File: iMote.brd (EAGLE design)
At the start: 50 x 50 mm, 47 parts, among them CN1 C-02235, CN2 ICSP, CN3 CC-HEADER, IC1 ATmega328P-AU, IC2 FT232RLSSOP, IC3 BLE112-A-VISUAL, Q1 16MHz, T1 2SC1815

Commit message: 5cmx5cmにおさまった!
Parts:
- C10: device rcl:E2,5-5 -> my:E2-5
- moved S1 31.1 mm to (37.3, 5.79), turned to 0 degrees
- moved R4 28.4 mm to (32.3, 41.1)
- moved S2 23.4 mm to (43.6, 17.2), turned to 90 degrees
- moved C11 19.6 mm to (24.3, 25.4)
- moved R1 18.1 mm to (33.0, 10.1), turned to 180 degrees
- moved C2 17.8 mm to (4.14, 8.85), turned to 0 degrees
- moved C1 16.0 mm to (4.13, 14.0), turned to 0 degrees
- moved C5 14.1 mm to (25.5, 11.5), turned to 180 degrees
- moved C3 14.0 mm to (25.5, 13.1), turned to 180 degrees
- moved PL-IRM1 13.8 mm to (13.9, 5.50)
- moved R9 13.3 mm to (20.2, 5.40), turned to 0 degrees
- moved R8 12.6 mm to (11.6, 43.0)
- moved LED6 12.5 mm to (11.6, 46.3), turned to 90 degrees
- moved C12 11.5 mm to (17.9, 4.49), turned to 270 degrees
- moved SJ1 11.2 mm to (38.5, 47.0), turned to 0 degrees
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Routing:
- net GND: track 0.00 -> 101.4 mm, vias 0 -> 11
- net +5V: track 0.00 -> 88.7 mm
- net +3V3: track 0.00 -> 73.9 mm
- net !RESET: track 0.00 -> 41.4 mm, vias 0 -> 2
- net !BLE/RST: track 0.00 -> 35.6 mm, vias 0 -> 2
- net D6/BLERX: track 0.00 -> 24.2 mm, vias 0 -> 2
- net BLE/P2_2: track 0.00 -> 23.3 mm, vias 0 -> 2
- net D7/BLETX: track 0.00 -> 23.0 mm, vias 0 -> 2
- net D0/USBRX: track 0.00 -> 20.1 mm, vias 0 -> 2
- net BLE/P2_1: track 0.00 -> 20.1 mm, vias 0 -> 1
- net N$8: track 0.00 -> 16.5 mm, vias 0 -> 2
- net D1/USBTX: track 0.00 -> 15.7 mm
- net D12/MISO: track 0.00 -> 13.5 mm, vias 0 -> 2
- net D11/MOSI: track 0.00 -> 13.5 mm
- net N$2: track 0.00 -> 11.9 mm
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
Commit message: いい感じや
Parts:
- moved SJ1 6.18 mm to (37.4, 40.9), turned to 270 degrees
- moved LED3 4.99 mm to (44.5, 40.6), turned to 0 degrees
- moved R5 4.12 mm to (41.0, 40.5)
- moved R6 3.14 mm to (37.0, 19.5)
- moved LED4 3.02 mm to (37.0, 16.4)
- moved C6 2.53 mm to (19.4, 35.0), turned to 270 degrees
- moved S2 1.90 mm to (41.8, 16.6)
- moved R2 1.39 mm to (5.32, 41.4), turned to 90 degrees
- moved LED1 1.17 mm to (3.36, 41.4), turned to 270 degrees
- moved C11 1.10 mm to (25.4, 25.4)
- moved C8 0.22 mm to (44.5, 37.8)
- moved CN1 0.10 mm to (17.4, 44.5)
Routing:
- net GND: track 101.4 -> 70.0 mm, vias 11 -> 13
- net BLE/P2_1: track 20.1 -> 38.5 mm, vias 1 -> 0
- net USBD-: track 3.94 -> 19.1 mm
- net +5V: track 88.7 -> 97.5 mm
- net +3V3: track 73.9 -> 65.9 mm
- net !RESET: track 41.4 -> 46.5 mm
- net BLE/P0_0: track 5.90 -> 3.00 mm
- net !BLE/RST: track 35.6 -> 37.8 mm
- net USB/TXLED: track 9.54 -> 11.5 mm
- net D12/MISO: track 13.5 -> 11.7 mm, vias 2 -> 1
- net BLE/P2_2: track 23.3 -> 21.7 mm, vias 2 -> 1
- net D7/BLETX: track 23.0 -> 22.3 mm

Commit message: CN3ひっくり返したらもうちょいよくなった
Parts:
- moved SJ1 13.5 mm to (24.1, 38.7)
- moved R4 6.46 mm to (38.5, 42.9)
- moved CN3 1.69 mm to (29.4, 44.1), turned to 180 degrees
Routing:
- net BLE/P2_1: track 38.5 -> 11.9 mm, vias 0 -> 1
- net !BLE/RST: track 37.8 -> 56.5 mm, vias 2 -> 0
- net BLE/P2_2: track 21.7 -> 15.5 mm, vias 1 -> 0
- net PRG/VDD: track 3.86 -> 6.69 mm
- net +3V3: track 65.9 -> 63.9 mm

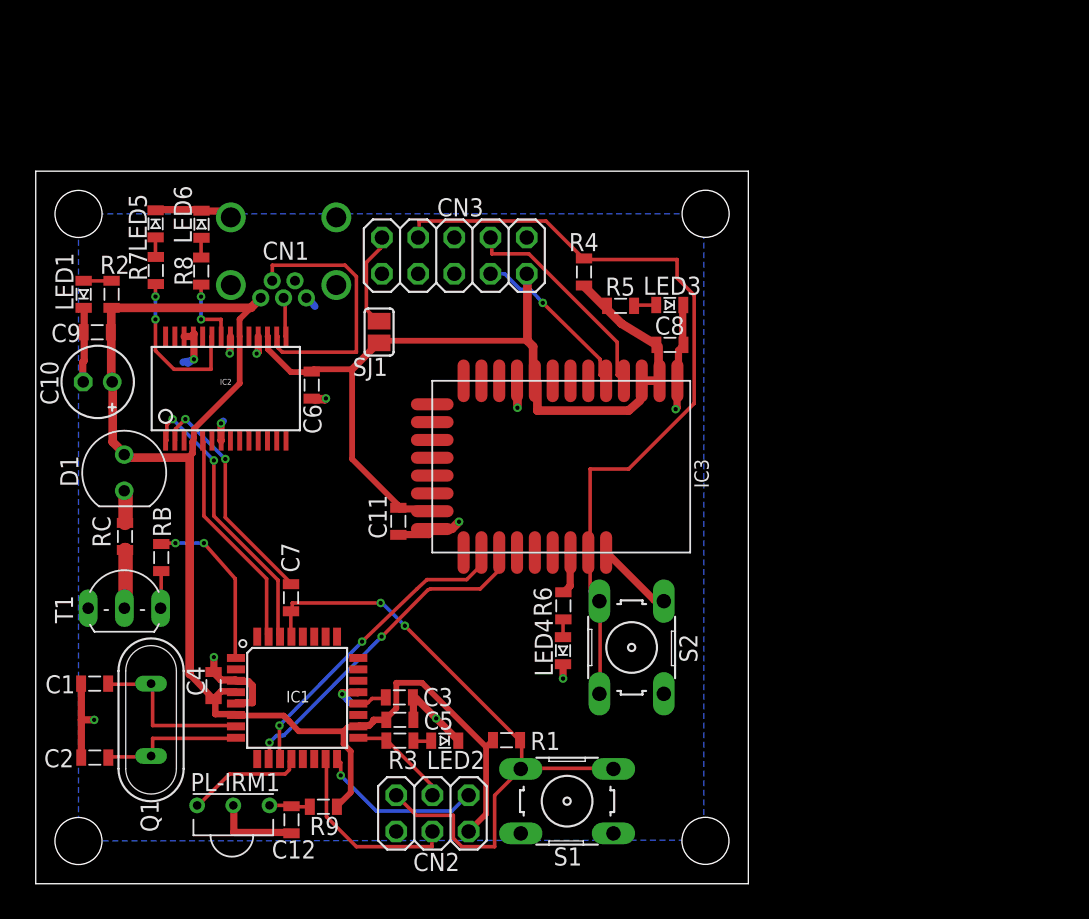
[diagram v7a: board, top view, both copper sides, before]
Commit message: CN2周り微調整
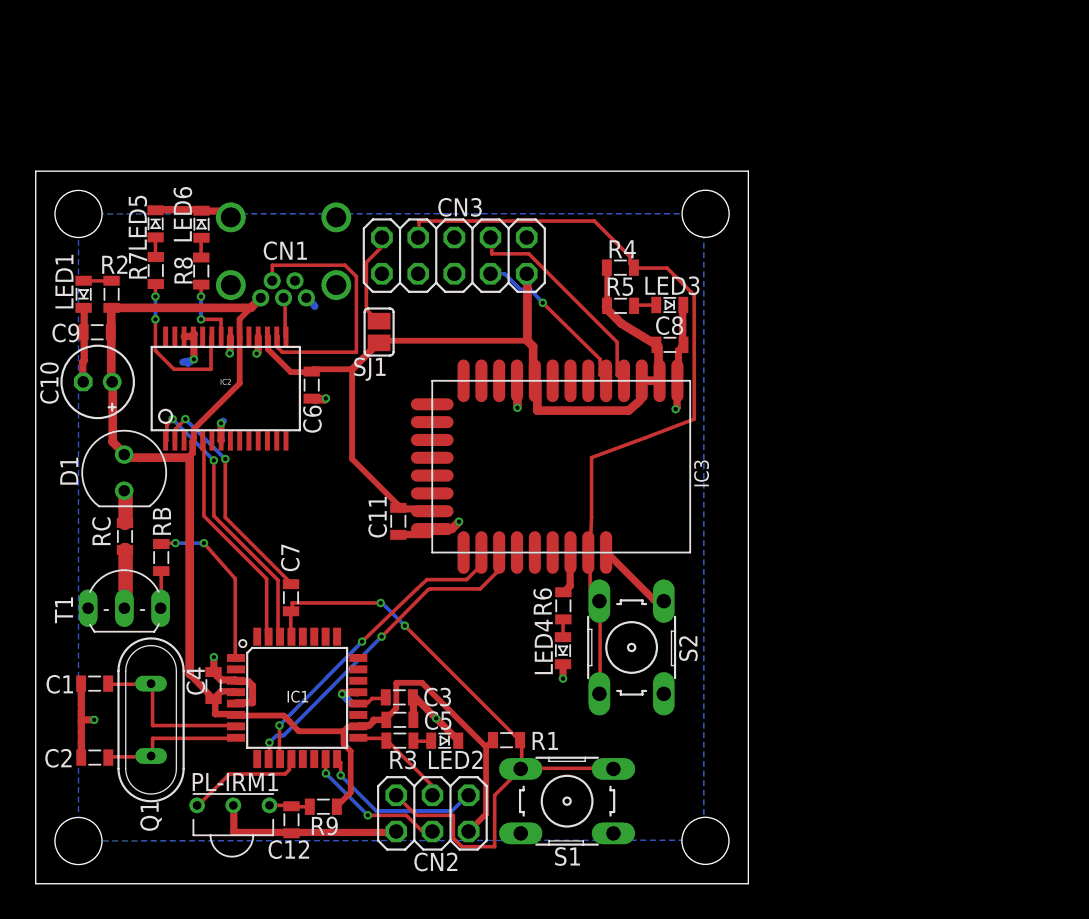
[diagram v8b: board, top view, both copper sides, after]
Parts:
- moved R4 2.57 mm to (41.0, 43.2), turned to 180 degrees
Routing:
- net GND: track 70.0 -> 77.3 mm
- net D11/MOSI: track 13.4 -> 10.2 mm, vias 0 -> 2
- net +3V3: track 63.9 -> 64.5 mm
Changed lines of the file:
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@@
 <attribute name="VALUE" x="43.738" y="35.526" size="1.27" layer="27"/>
 </element>
-<element name="R4" library="my" package="2012" value="1K" x="38.47" y="42.926" smashed="yes" rot="R270">
-<attribute name="NAME" x="37.412" y="44.386" size="1.27" layer="25"/>
-<attribute name="VALUE" x="36.184" y="43.688" size="1.27" layer="27" rot="R270"/>
+<element name="R4" library="my" package="2012" value="1K" x="41.026" y="43.23" smashed="yes" rot="R180">
+<attribute name="NAME" x="40.112" y="43.886" size="1.27" layer="25"/>
+<attribute name="VALUE" x="41.788" y="45.516" size="1.27" layer="27" rot="R180"/>
 </element>
 <element name="S2" library="switch-omron" package="B3F-10XX" value="B3F-1000" x="41.812" y="16.578" smashed="yes" rot="R90">
@@
 </element>
 <element name="C12" library="my" package="2012" value="4.7uF" x="17.944" y="4.488" smashed="yes" rot="R270">
-<attribute name="NAME" x="19.65" y="3.04" size="1.27" layer="25" rot="R180"/>
+<attribute name="NAME" x="16.25" y="1.76" size="1.27" layer="25"/>
 <attribute name="VALUE" x="15.658" y="5.25" size="1.27" layer="27" rot="R270"/>
 </element>
@@
 <contactref element="IC1" pad="15"/>
 <contactref element="CN2" pad="4"/>
-<wire x1="20.4" y1="4.7" x2="20.4" y2="8.7" width="0.254" layer="1"/>
-<wire x1="22.5" y1="2.6" x2="20.4" y2="4.7" width="0.254" layer="1"/>
-<wire x1="27.8" y1="2.6" x2="22.5" y2="2.6" width="0.254" layer="1"/>
-<wire x1="27.8" y1="3.6" x2="27.8" y2="2.6" width="0.254" layer="1"/>
-<wire x1="20.4" y1="8.7" x2="20.342" y2="8.7494" width="0.254" layer="1"/>
-<wire x1="27.8" y1="3.6" x2="27.834" y2="3.668" width="0.254" layer="1"/>
+<wire x1="20.342" y1="8.7494" x2="20.342" y2="7.742" width="0.254" layer="1"/>
+<wire x1="20.342" y1="7.742" x2="20.36" y2="7.74" width="0.254" layer="1"/>
+<via x="20.36" y="7.74" extent="1-16" drill="0.3"/>
+<wire x1="20.36" y1="7.74" x2="23.3" y2="4.8" width="0.254" layer="16"/>
+<via x="23.3" y="4.8" extent="1-16" drill="0.3"/>
+<wire x1="23.3" y1="4.8" x2="26" y2="4.8" width="0.254" layer="1"/>
+<wire x1="26" y1="4.8" x2="27.1" y2="3.7" width="0.254" layer="1"/>
+<wire x1="27.1" y1="3.7" x2="27.802" y2="3.7" width="0.254" layer="1"/>
+<wire x1="27.802" y1="3.7" x2="27.834" y2="3.668" width="0.254" layer="1"/>
 </signal>
 <signal name="D12/MISO">
@@
 <wire x1="22" y1="12.8" x2="21.999459375" y2="12.799465625" width="0.508" layer="16"/>
 <wire x1="22" y1="12.8" x2="22.140240625" y2="12.661178125" width="0.508" layer="16"/>
+<wire x1="18.2" y1="3.6" x2="25.2" y2="3.6" width="0.508" layer="1"/>
+<wire x1="25.2" y1="3.6" x2="25.294" y2="3.668" width="0.508" layer="1"/>
+<wire x1="18.2" y1="3.6" x2="17.944" y2="3.538" width="0.508" layer="1"/>
 </signal>
 <signal name="N$10">
@@
 <wire x1="42.4" y1="35.1" x2="42.522" y2="35.29" width="0.4064" layer="1"/>
 <wire x1="35.2" y1="35.2" x2="35.022" y2="35.29" width="0.4064" layer="1"/>
-<wire x1="39.9" y1="40.5" x2="38.5" y2="41.9" width="0.6096" layer="1"/>
-<wire x1="38.5" y1="41.9" x2="38.47" y2="41.976" width="0.4064" layer="1"/>
 <wire x1="39.9" y1="40.5" x2="40.086" y2="40.55" width="0.4064" layer="1"/>
 <wire x1="34.5" y1="38.1" x2="34.5" y2="42.8" width="0.6096" layer="1"/>
@@
 <wire x1="24.2" y1="38.1" x2="34.5" y2="38.1" width="0.4064" layer="1"/>
 <wire x1="24.2" y1="38.1" x2="24.092" y2="37.95" width="0.4064" layer="1"/>
+<wire x1="40.1" y1="40.7" x2="40.1" y2="43.2" width="0.4064" layer="1"/>
+<wire x1="40.1" y1="43.2" x2="40.076" y2="43.23" width="0.4064" layer="1"/>
+<wire x1="40.1" y1="40.7" x2="40.086" y2="40.55" width="0.4064" layer="1"/>
 </signal>
 <signal name="!BLE/RST">
@@
 <wire x1="39.5" y1="19.9" x2="39.5514" y2="19.8292" width="0.254" layer="1"/>
 <wire x1="38.9" y1="23.2" x2="38.772" y2="23.24" width="0.254" layer="1"/>
-<wire x1="35.8" y1="46.5" x2="38.4" y2="43.9" width="0.254" layer="1"/>
-<wire x1="26.9" y1="46.5" x2="35.8" y2="46.5" width="0.254" layer="1"/>
+<wire x1="41.7" y1="43.5" x2="41.9" y2="43.3" width="0.254" layer="1"/>
+<wire x1="41.7" y1="44" x2="41.7" y2="43.5" width="0.254" layer="1"/>
+<wire x1="39.2" y1="46.5" x2="41.7" y2="44" width="0.254" layer="1"/>
+<wire x1="26.9" y1="46.5" x2="39.2" y2="46.5" width="0.254" layer="1"/>
 <wire x1="26.9" y1="45.4" x2="26.9" y2="46.5" width="0.254" layer="1"/>
-<wire x1="38.4" y1="43.9" x2="38.47" y2="43.876" width="0.254" layer="1"/>
+<wire x1="41.9" y1="43.3" x2="41.976" y2="43.23" width="0.254" layer="1"/>
 <wire x1="26.9" y1="45.4" x2="26.832" y2="45.342" width="0.254" layer="1"/>
-<wire x1="45" y1="43.8" x2="38.5" y2="43.8" width="0.254" layer="1"/>
-<wire x1="45" y1="42.5" x2="45" y2="43.8" width="0.254" layer="1"/>
-<wire x1="46.2" y1="41.3" x2="45" y2="42.5" width="0.254" layer="1"/>
-<wire x1="46.2" y1="33.7" x2="46.2" y2="41.3" width="0.254" layer="1"/>
-<wire x1="41.6" y1="29.1" x2="46.2" y2="33.7" width="0.254" layer="1"/>
-<wire x1="38.9" y1="29.1" x2="41.6" y2="29.1" width="0.254" layer="1"/>
-<wire x1="38.9" y1="23.3" x2="38.9" y2="29.1" width="0.254" layer="1"/>
-<wire x1="38.5" y1="43.8" x2="38.47" y2="43.876" width="0.254" layer="1"/>
+<wire x1="39" y1="25.7" x2="38.9" y2="23.3" width="0.254" layer="1"/>
+<wire x1="39" y1="29.9" x2="39" y2="25.7" width="0.254" layer="1"/>
+<wire x1="42.8" y1="31.3" x2="39" y2="29.9" width="0.254" layer="1"/>
+<wire x1="46.2" y1="32.6" x2="42.8" y2="31.3" width="0.254" layer="1"/>
+<wire x1="46.2" y1="41.3" x2="46.2" y2="32.6" width="0.254" layer="1"/>
+<wire x1="44.3" y1="43.2" x2="46.2" y2="41.3" width="0.254" layer="1"/>
+<wire x1="42.1" y1="43.2" x2="44.3" y2="43.2" width="0.254" layer="1"/>
 <wire x1="38.9" y1="23.3" x2="38.772" y2="23.24" width="0.254" layer="1"/>
+<wire x1="42.1" y1="43.2" x2="41.976" y2="43.23" width="0.254" layer="1"/>
 </signal>
 <signal name="N$5">
